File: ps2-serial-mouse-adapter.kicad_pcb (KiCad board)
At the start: 2 copper layers, 72.4 x 31.7 mm, 10 parts, among them J4 DB9_Female, U1 Arduino_Mini, U2 MAX232

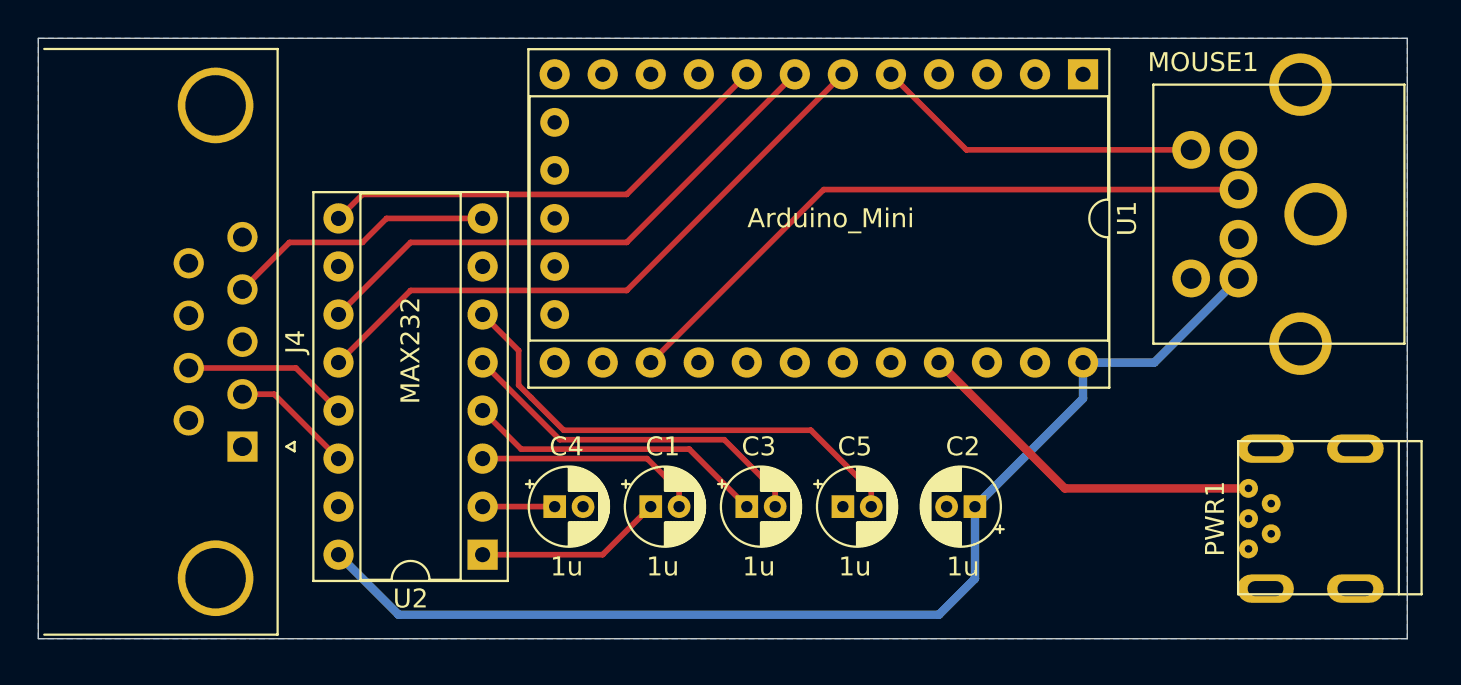
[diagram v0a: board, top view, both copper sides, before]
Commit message: Shrink PCB
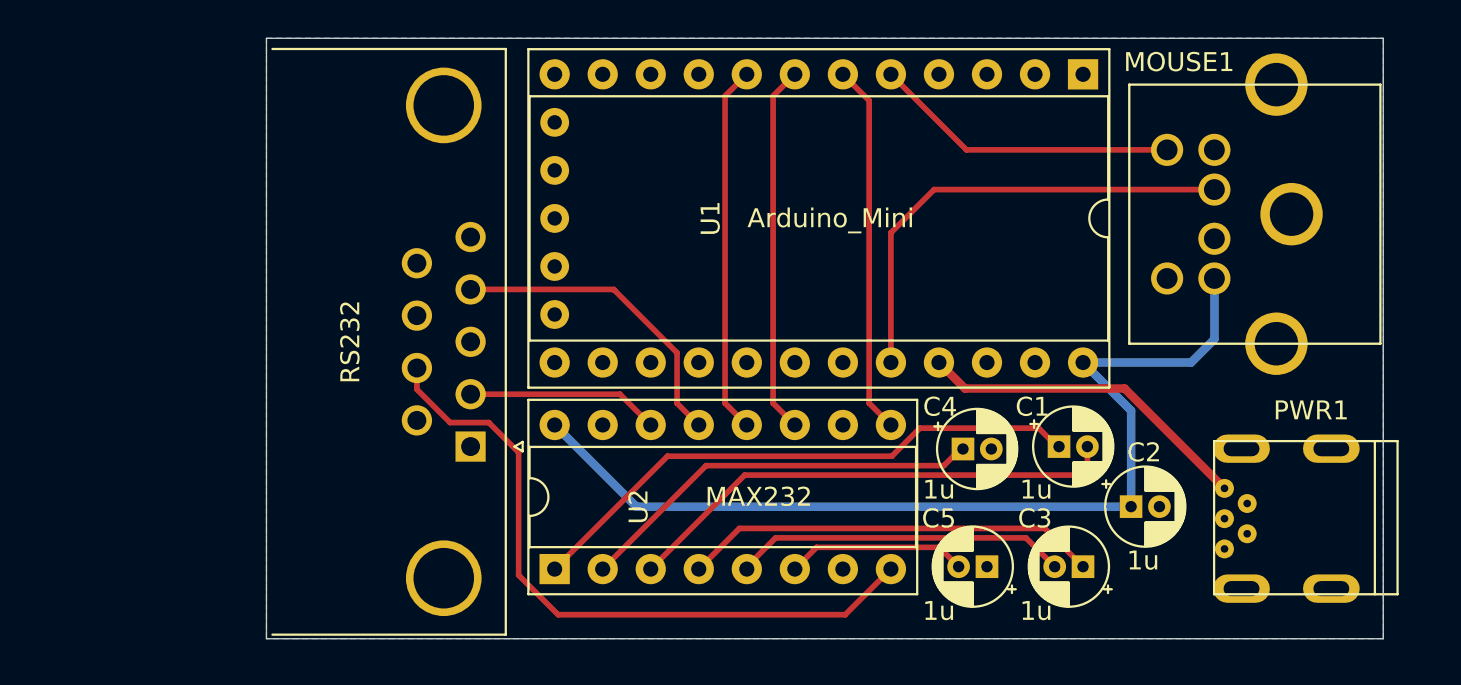
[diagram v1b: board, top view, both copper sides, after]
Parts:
- moved C1 21.8 mm to (129.5, 73.7)
- moved C4 21.8 mm to (124.5, 73.8)
- moved C3 18.1 mm to (130.8, 80.0), turned to 180 degrees
- moved RS232 12.1 mm to (98.4, 73.7)
- moved C5 8.26 mm to (125.7, 80.0), turned to 180 degrees
- moved C2 8.25 mm to (133.3, 76.8), turned to 0 degrees
- moved U2 3.89 mm to (102.9, 80.1), turned to 90 degrees
- moved MOUSE1 1.27 mm to (135.3, 64.8)
- moved PWR1 1.27 mm to (142.2, 77.5)
- renumbered J4 to RS232
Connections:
- RS232 pad 4: Net-(J4-Pad4) -> Net-(RS232-Pad4)
- RS232 pad 7: Net-(J4-Pad7) -> Net-(RS232-Pad7)
- U1 pad 15: DATA -> (no net)
- U1 pad 20: (no net) -> DATA
- U2 pad 12: RTS -> DTS
- U2 pad 13: Net-(J4-Pad7) -> Net-(RS232-Pad4)
- U2 pad 8: Net-(J4-Pad4) -> Net-(RS232-Pad7)
- U2 pad 9: DTS -> RTS
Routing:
- net Net-(RS232-Pad7): track 0.00 -> 35.9 mm
- net Net-(C1-Pad1): track 9.94 -> 30.1 mm
- net Net-(C4-Pad1): track 3.81 -> 21.6 mm
- net Net-(C5-Pad2): track 26.4 -> 9.56 mm
- net Net-(RS232-Pad4): track 0.00 -> 16.6 mm
- net Net-(C1-Pad2): track 11.9 -> 26.3 mm
- net Net-(J4-Pad4): track 14.3 -> 0.00 mm
- net RTS: track 33.0 -> 19.6 mm
- net DATA: track 34.9 -> 24.9 mm
- net TX: track 29.4 -> 19.5 mm
- net Net-(J4-Pad7): track 8.85 -> 0.00 mm
- net Net-(C2-Pad1): track 59.6 -> 51.6 mm
- net Net-(C3-Pad1): track 16.1 -> 22.0 mm
- net DTS: track 24.7 -> 19.5 mm
- net Net-(RS232-Pad2): track 6.90 -> 10.2 mm
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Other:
- board size 72.4 x 31.7 mm -> 59.1 x 31.7 mm
- net class Power: clearance 0.35 -> 0.3

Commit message: Update PWR1
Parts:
- moved PWR1 4.45 mm to (137.8, 77.5), turned to 90 degrees
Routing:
- net VCC: track 17.9 -> 21.4 mm
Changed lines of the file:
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@@
     (thickness 1.6)
     (drawings 4)
-    (tracks 61)
+    (tracks 63)
     (zones 0)
     (modules 10)
@@
     (add_net "Net-(C4-Pad1)")
     (add_net "Net-(C5-Pad2)")
-    (add_net "Net-(MOUSE1-Pad2)")
-    (add_net "Net-(MOUSE1-Pad6)")
-    (add_net "Net-(PWR1-Pad2)")
-    (add_net "Net-(PWR1-Pad3)")
-    (add_net "Net-(PWR1-Pad4)")
-    (add_net "Net-(RS232-Pad1)")
     (add_net "Net-(RS232-Pad2)")
-    (add_net "Net-(RS232-Pad3)")
     (add_net "Net-(RS232-Pad4)")
-    (add_net "Net-(RS232-Pad6)")
     (add_net "Net-(RS232-Pad7)")
-    (add_net "Net-(RS232-Pad8)")
-    (add_net "Net-(RS232-Pad9)")
-    (add_net "Net-(U1-Pad1)")
-    (add_net "Net-(U1-Pad10)")
-    (add_net "Net-(U1-Pad11)")
-    (add_net "Net-(U1-Pad12)")
-    (add_net "Net-(U1-Pad13)")
-    (add_net "Net-(U1-Pad14)")
-    (add_net "Net-(U1-Pad15)")
-    (add_net "Net-(U1-Pad16)")
-    (add_net "Net-(U1-Pad17)")
-    (add_net "Net-(U1-Pad18)")
-    (add_net "Net-(U1-Pad19)")
-    (add_net "Net-(U1-Pad2)")
-    (add_net "Net-(U1-Pad22)")
-    (add_net "Net-(U1-Pad26)")
-    (add_net "Net-(U1-Pad27)")
-    (add_net "Net-(U1-Pad28)")
-    (add_net "Net-(U1-Pad29)")
-    (add_net "Net-(U1-Pad3)")
-    (add_net "Net-(U1-Pad9)")
-    (add_net "Net-(U2-Pad10)")
-    (add_net "Net-(U2-Pad7)")
     (add_net RTS)
     (add_net TX)
@@
   )
   (module MyLibrary:USB_Mini-B-Jing_Extension_LSCS_C46398 (layer F.Cu)
-    (at 142.24 77.47 270)
+    (at 137.795 77.47 90)
     (fp_text reference PWR1 (at -5.715 -0.635 180) (layer F.SilkS)
       (effects (font (size 1 1) (thickness 0.15)))
@@
       (effects (font (size 1 1) (thickness 0.15)))
     )
-    (fp_line (start -4.1 -5.2) (end 4 -5.2) (layer F.SilkS) (width 0.12))
-    (fp_line (start -4.1 4.5) (end -4.1 -5.2) (layer F.SilkS) (width 0.12))
-    (fp_line (start 4 4.5) (end -4.1 4.5) (layer F.SilkS) (width 0.12))
-    (fp_line (start 4 -5.2) (end 4 4.5) (layer F.SilkS) (width 0.12))
-    (fp_line (start 4 -4) (end -4.1 -4) (layer F.SilkS) (width 0.12))
-    (pad 2 thru_hole circle (at -0.8 2.75 180) (size 1 1) (drill 0.4) (layers *.Cu *.Mask))
-    (pad 4 thru_hole circle (at 0.8 2.75 180) (size 1 1) (drill 0.4) (layers *.Cu *.Mask))
-    (pad 5 thru_hole circle (at 1.6 3.95 180) (size 1 1) (drill 0.4) (layers *.Cu *.Mask)
-      (net 3 GND))
-    (pad 1 thru_hole circle (at -1.6 3.95 180) (size 1 1) (drill 0.4) (layers *.Cu *.Mask)
+    (fp_line (start -3.7 7.45) (end 3.7 7.45) (layer F.SilkS) (width 0.12))
+    (fp_line (start -3.7 9.7) (end -3.7 0) (layer F.SilkS) (width 0.12))
+    (fp_line (start -3.7 9.7) (end 3.7 9.7) (layer F.SilkS) (width 0.12))
+    (fp_line (start 3.7 0) (end 3.7 9.7) (layer F.SilkS) (width 0.12))
+    (fp_line (start -3.7 0) (end 3.7 0) (layer F.SilkS) (width 0.12))
+    (pad 6 thru_hole oval (at 3.7 5.65 90) (size 1.4 2.5) (drill oval 0.8 1.9) (layers *.Cu *.Mask)
+      (net 3 GND))
+    (pad 6 thru_hole oval (at -3.7 5.65 90) (size 1.4 2.5) (drill oval 0.8 1.9) (layers *.Cu *.Mask)
+      (net 3 GND))
+    (pad 6 thru_hole oval (at -3.7 0.9 90) (size 1.4 2.5) (drill oval 0.8 1.9) (layers *.Cu *.Mask)
+      (net 3 GND))
+    (pad 6 thru_hole oval (at 3.7 0.9 90) (size 1.4 2.5) (drill oval 0.8 1.9) (layers *.Cu *.Mask)
+      (net 3 GND))
+    (pad 4 thru_hole circle (at 0.8 1.2 90) (size 1.1 1.1) (drill 0.4) (layers *.Cu *.Mask))
+    (pad 2 thru_hole circle (at -0.8 1.2 90) (size 1.1 1.1) (drill 0.4) (layers *.Cu *.Mask))
+    (pad 1 thru_hole circle (at -1.6 0 90) (size 1.1 1.1) (drill 0.4) (layers *.Cu *.Mask)
       (net 9 VCC))
-    (pad 3 thru_hole circle (at 0 3.95 180) (size 1 1) (drill 0.4) (layers *.Cu *.Mask))
-    (pad 6 thru_hole oval (at 3.7 3.05 180) (size 3 1.5) (drill oval 1.9 0.8) (layers *.Cu *.Mask)
-      (net 3 GND))
-    (pad 6 thru_hole oval (at -3.7 3.05 180) (size 3 1.5) (drill oval 1.9 0.8) (layers *.Cu *.Mask)
-      (net 3 GND))
-    (pad 6 thru_hole oval (at -3.7 -1.7 180) (size 3 1.5) (drill oval 1.9 0.8) (layers *.Cu *.Mask)
-      (net 3 GND))
-    (pad 6 thru_hole oval (at 3.7 -1.7 180) (size 3 1.5) (drill oval 1.9 0.8) (layers *.Cu *.Mask)
-      (net 3 GND))
+    (pad 5 thru_hole circle (at 1.6 0 90) (size 1.1 1.1) (drill 0.4) (layers *.Cu *.Mask)
+      (net 3 GND))
+    (pad 3 thru_hole circle (at 0 0 90) (size 1.1 1.1) (drill 0.4) (layers *.Cu *.Mask))
   )
   (module Capacitor_THT:CP_Radial_D4.0mm_P1.50mm (layer F.Cu)
@@
   (segment (start 123.206999 78.986999) (end 116.720001 78.986999) (width 0.3) (layer F.Cu) (net 8))
   (segment (start 124.23 80.01) (end 123.206999 78.986999) (width 0.3) (layer F.Cu) (net 8))
-  (segment (start 133.010001 70.590001) (end 138.29 75.87) (width 0.45) (layer F.Cu) (net 9))
-  (segment (start 124.565001 70.590001) (end 133.010001 70.590001) (width 0.45) (layer F.Cu) (net 9))
   (segment (start 123.19 69.215) (end 124.565001 70.590001) (width 0.45) (layer F.Cu) (net 9))
+  (segment (start 124.565001 70.590001) (end 133.879999 70.590001) (width 0.45) (layer F.Cu) (net 9))
+  (segment (start 136.719999 77.994999) (end 137.795 79.07) (width 0.45) (layer F.Cu) (net 9))
+  (segment (start 136.719999 73.430001) (end 136.719999 77.994999) (width 0.45) (layer F.Cu) (net 9))
+  (segment (start 133.879999 70.590001) (end 136.719999 73.430001) (width 0.45) (layer F.Cu) (net 9))
   (segment (start 120.65 53.975) (end 124.645 57.97) (width 0.3) (layer F.Cu) (net 10))
   (segment (start 124.645 57.97) (end 135.255 57.97) (width 0.3) (layer F.Cu) (net 10))
@@
   (segment (start 120.65 69.215) (end 120.65 62.357) (width 0.3) (layer F.Cu) (net 11))
   (segment (start 122.937 60.07) (end 137.755 60.07) (width 0.3) (layer F.Cu) (net 11))
+  (segment (start 114.419999 55.125001) (end 115.57 53.975) (width 0.3) (layer F.Cu) (net 12))
+  (segment (start 114.419999 71.366999) (end 114.419999 55.125001) (width 0.3) (layer F.Cu) (net 12))
+  (segment (start 115.57 72.517) (end 114.419999 71.366999) (width 0.3) (layer F.Cu) (net 12))
+  (segment (start 111.879999 55.125001) (end 113.03 53.975) (width 0.3) (layer F.Cu) (net 13))
+  (segment (start 111.879999 71.366999) (end 111.879999 55.125001) (width 0.3) (layer F.Cu) (net 13))
+  (segment (start 113.03 72.517) (end 111.879999 71.366999) (width 0.3) (layer F.Cu) (net 13))
+  (segment (start 119.499999 55.364999) (end 118.11 53.975) (width 0.3) (layer F.Cu) (net 14))
+  (segment (start 119.499999 71.366999) (end 119.499999 55.364999) (width 0.3) (layer F.Cu) (net 14))
+  (segment (start 120.65 72.517) (end 119.499999 71.366999) (width 0.3) (layer F.Cu) (net 14))
   (segment (start 118.237 82.55) (end 120.65 80.137) (width 0.3) (layer F.Cu) (net 15))
   (segment (start 103.052998 82.55) (end 118.237 82.55) (width 0.3) (layer F.Cu) (net 15))
@@
   (segment (start 106.323 70.89) (end 107.95 72.517) (width 0.3) (layer F.Cu) (net 17))
   (segment (start 98.425 70.89) (end 106.323 70.89) (width 0.3) (layer F.Cu) (net 17))
-  (segment (start 114.419999 55.125001) (end 115.57 53.975) (width 0.3) (layer F.Cu) (net 12))
-  (segment (start 114.419999 71.366999) (end 114.419999 55.125001) (width 0.3) (layer F.Cu) (net 12))
-  (segment (start 115.57 72.517) (end 114.419999 71.366999) (width 0.3) (layer F.Cu) (net 12))
-  (segment (start 111.879999 55.125001) (end 113.03 53.975) (width 0.3) (layer F.Cu) (net 13))
-  (segment (start 111.879999 71.366999) (end 111.879999 55.125001) (width 0.3) (layer F.Cu) (net 13))
-  (segment (start 113.03 72.517) (end 111.879999 71.366999) (width 0.3) (layer F.Cu) (net 13))
-  (segment (start 119.499999 55.364999) (end 118.11 53.975) (width 0.3) (layer F.Cu) (net 14))
-  (segment (start 119.499999 71.366999) (end 119.499999 55.364999) (width 0.3) (layer F.Cu) (net 14))
-  (segment (start 120.65 72.517) (end 119.499999 71.366999) (width 0.3) (layer F.Cu) (net 14))
   (zone (net 3) (net_name GND) (layer B.Cu) (hatch edge 0.508)
     (connect_pads (clearance 0.508))
     (min_thickness 0.254)
-    (fill (arc_segments 32) (thermal_gap 0.508) (thermal_bridge_width 0.508))
+    (fill yes (arc_segments 32) (thermal_gap 0.508) (thermal_bridge_width 0.508))
     (polygon
       (pts

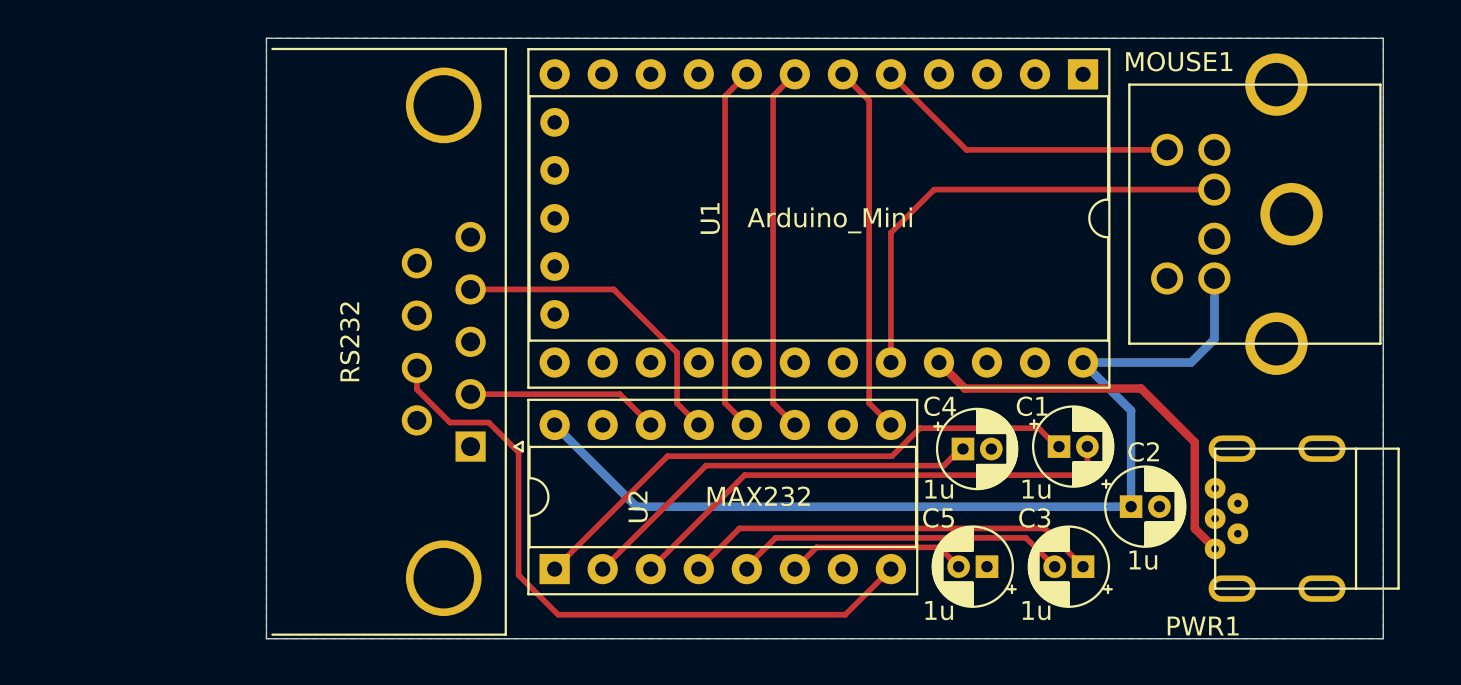
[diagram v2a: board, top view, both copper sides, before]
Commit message: Traces cleanup
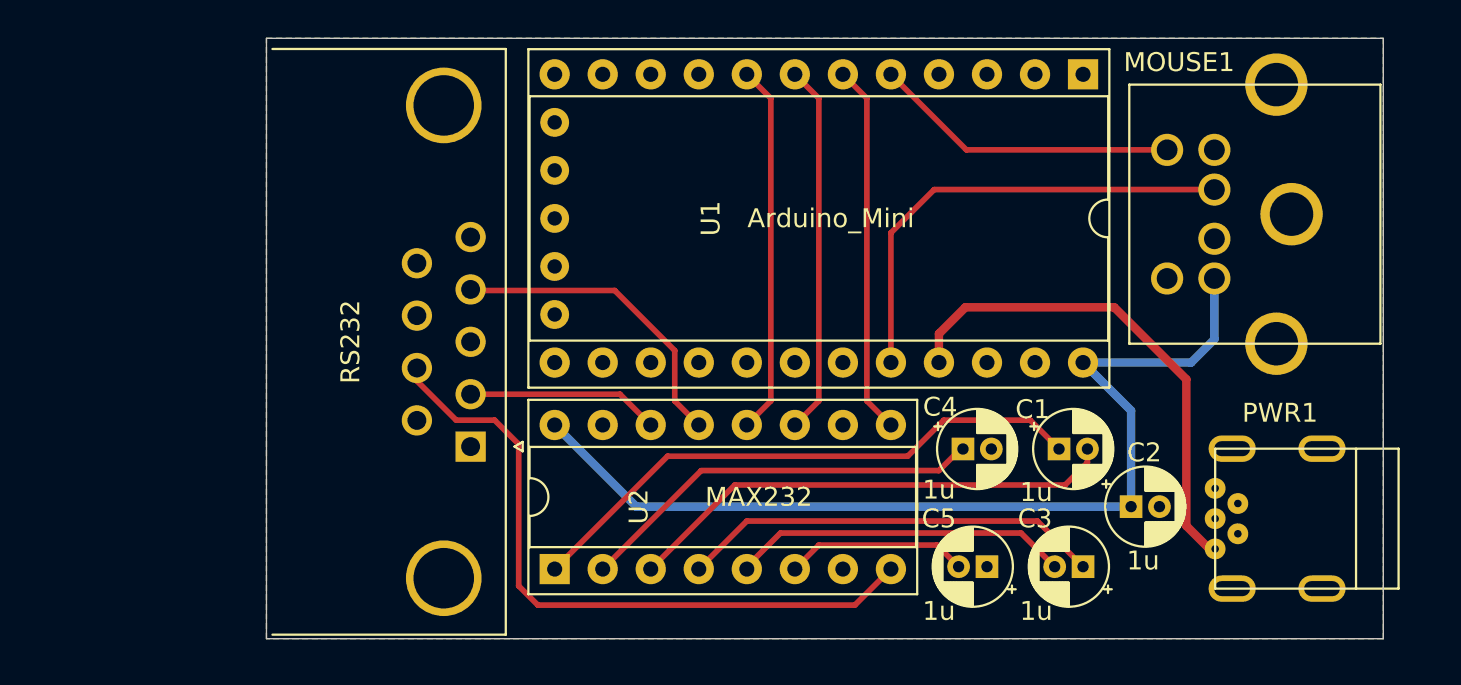
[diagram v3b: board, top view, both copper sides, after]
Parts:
- moved C1 0.13 mm to (129.5, 73.8)
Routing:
- net VCC: track 21.4 -> 26.5 mm
- net Net-(C1-Pad1): track 30.1 -> 30.6 mm
- added copper zone on F.Cu, net GND
